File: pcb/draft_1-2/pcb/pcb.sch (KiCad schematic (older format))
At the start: 26 parts, among them J1 USB4110-GF-A, U1 H3LIS200DLTR, U2 ATSAML21J16B-AUT, U3 BQ25155

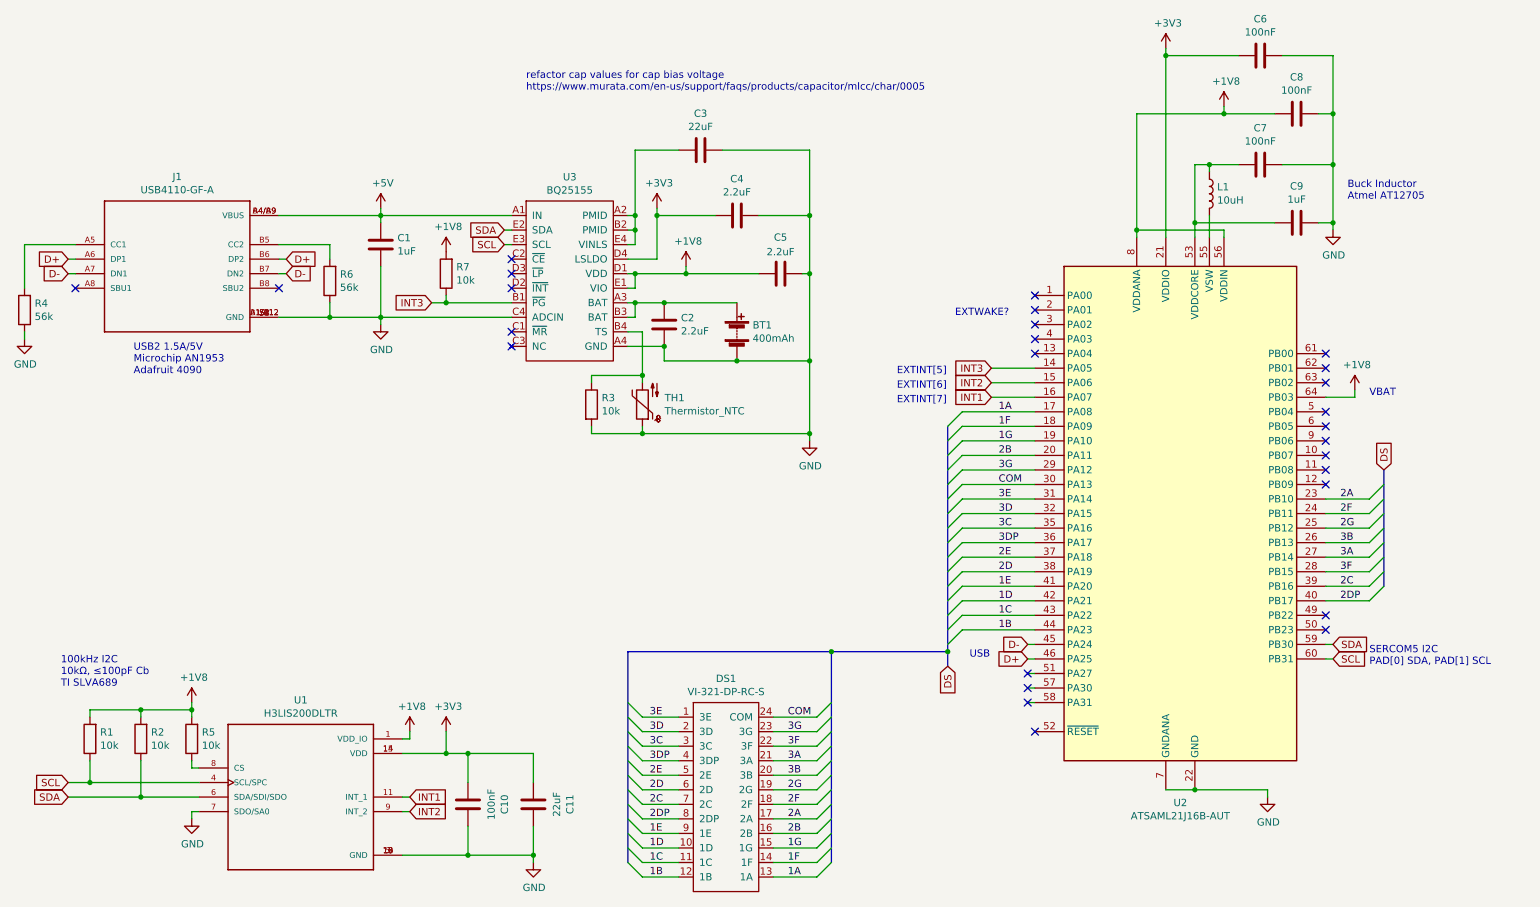
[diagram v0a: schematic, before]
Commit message: organized silk screen and swd tp
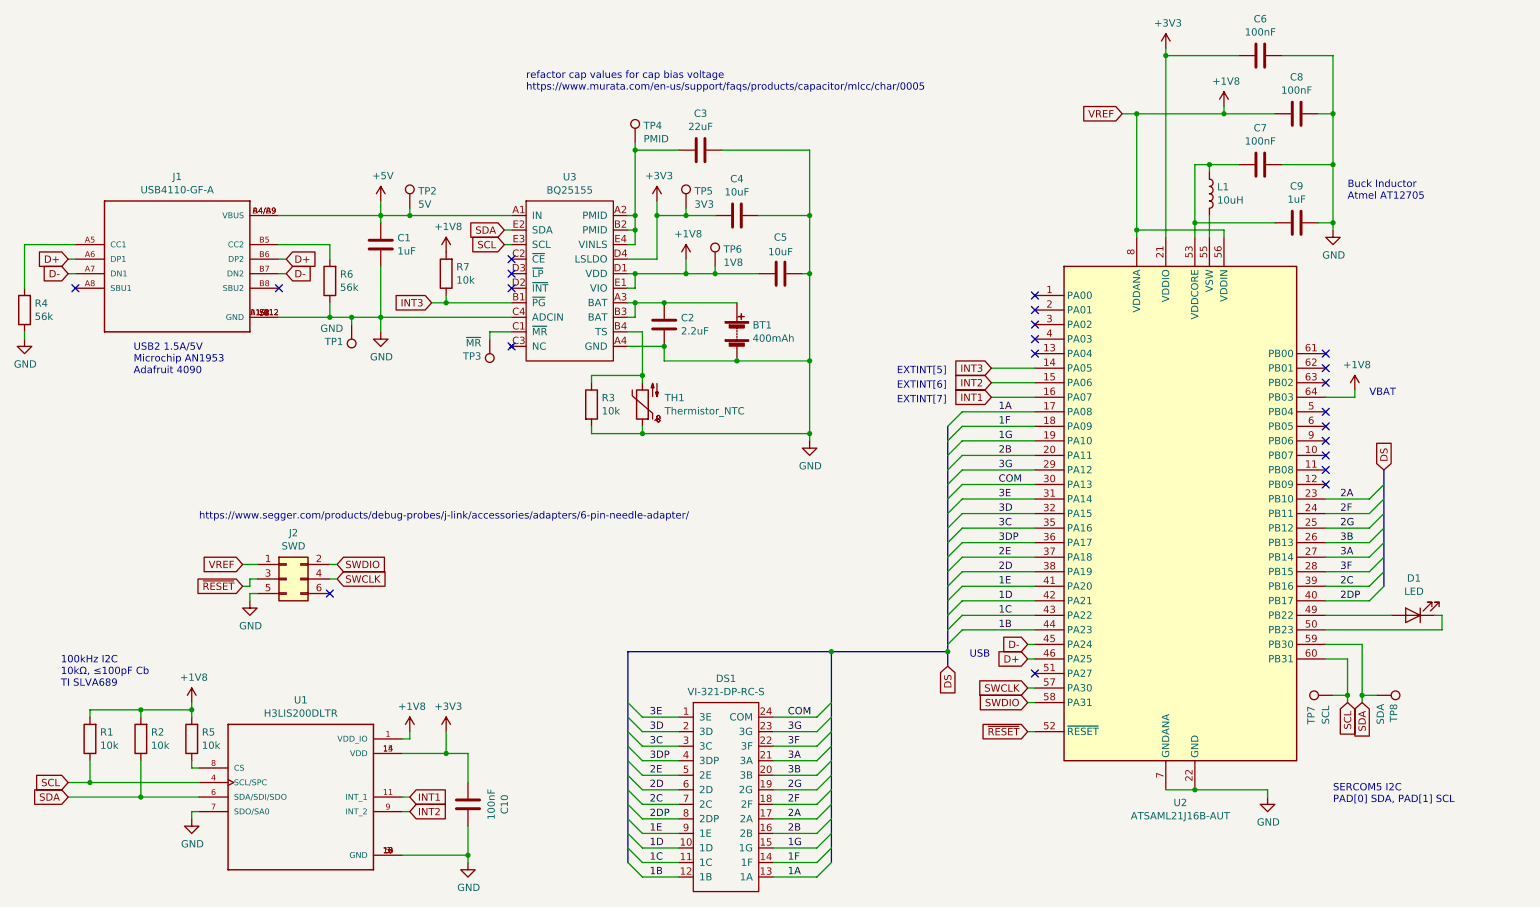
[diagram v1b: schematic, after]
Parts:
- removed C11: 22uF, Capacitor_SMD:C_0805_2012Metric, symbol Device:C
- added D1: LED, LED_SMD:LED_0603_1608Metric_Castellated, symbol Device:LED
- added J2: SWD, Connector_PinHeader_2.54mm:PinHeader_2x03_P2.54mm_Vertical, symbol Connector_Generic:Conn_02x03_Odd_Even
- added TP1: GND, symbol Connector:TestPoint
- added TP2: 5V, symbol Connector:TestPoint
- added TP3: ~MR, symbol Connector:TestPoint
- added TP4: PMID, symbol Connector:TestPoint
- added TP5: 3V3, symbol Connector:TestPoint
- added TP6: 1V8, symbol Connector:TestPoint
- added TP7: SCL, symbol Connector:TestPoint
- added TP8: SDA, symbol Connector:TestPoint
- C4, C5: value 2.2uF -> 10uF
- TH1: footprint Resistor_SMD:R_0402_1005Metric -> Connector_PinHeader_2.54mm:PinHeader_1x02_P2.54mm_Vertical
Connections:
- net +1V8: now also J2.1 (Pin_1), TP6.1
- net +3V3: now also TP5.1
- net +5V: now also TP2.1
- net GND: now also J2.5 (Pin_5), TP1.1
- net SCL: now also TP7.1
- net SDA: now also TP8.1
- net at C3.2, U3.A2 (PMID), U3.B2 (PMID)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: now also TP4.1
- net at U3.C1 (~MR): now also TP3.1
- net at U2.49 (PB22): now also D1.2 (A)
- net at U2.50 (PB23): now also D1.1 (K)
- net ~RESET: now reaches U2.52 (~RESET)
- net ~RESET: now also J2.3 (Pin_3)
- net SWCLK: now reaches U2.57 (PA30)
- net SWCLK: now also J2.4 (Pin_4)
- net SWDIO: now reaches U2.58 (PA31)
- net SWDIO: now also J2.2 (Pin_2)
- no-connect marks 27 -> 22
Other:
- note added: "https://www.segger.com/products/debug-probes/j-link/accessories/adapters/6-pin-needle-adapter/"
- note removed: "EXTWAKE?"

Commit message: add example image to readme
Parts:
- C1, C10, C2, C4, C5, C6, C7, C8, C9: footprint Capacitor_SMD:C_0402_1005Metric -> Capacitor_SMD:C_0805_2012Metric
- R1, R2, R3, R4, R5, R6, R7: footprint Resistor_SMD:R_0402_1005Metric -> Resistor_SMD:R_0805_2012Metric
- TP1, TP2, TP3, TP4, TP5, TP6, TP7, TP8: footprint (none) -> TestPoint:TestPoint_Pad_2.0x2.0mm
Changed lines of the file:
@@
 F 0 "R5" H 1930 5504 50  0000 R CNN
 F 1 "10k" H 1930 5595 50  0000 R CNN
-F 2 "Resistor_SMD:R_0402_1005Metric" V 1930 5550 50  0001 C CNN
+F 2 "Resistor_SMD:R_0805_2012Metric" V 1930 5550 50  0001 C CNN
 F 3 "~" H 2000 5550 50  0001 C CNN
 	1    2000 5550
@@
 F 0 "C1" H 3415 2196 50  0000 L CNN
 F 1 "1uF" H 3415 2105 50  0000 L CNN
-F 2 "Capacitor_SMD:C_0402_1005Metric" H 3338 2000 50  0001 C CNN
+F 2 "Capacitor_SMD:C_0805_2012Metric" H 3338 2000 50  0001 C CNN
 F 3 "~" H 3300 2150 50  0001 C CNN
 	1    3300 2150
@@
 F 0 "C5" V 6300 2350 50  0000 C CNN
 F 1 "10uF" V 6200 2350 50  0000 C CNN
-F 2 "Capacitor_SMD:C_0402_1005Metric" H 6088 2200 50  0001 C CNN
+F 2 "Capacitor_SMD:C_0805_2012Metric" H 6088 2200 50  0001 C CNN
 F 3 "~" H 6050 2350 50  0001 C CNN
 	1    6050 2350
@@
 F 0 "C2" H 5365 2746 50  0000 L CNN
 F 1 "2.2uF" H 5365 2655 50  0000 L CNN
-F 2 "Capacitor_SMD:C_0402_1005Metric" H 5288 2550 50  0001 C CNN
+F 2 "Capacitor_SMD:C_0805_2012Metric" H 5288 2550 50  0001 C CNN
 F 3 "~" H 5250 2700 50  0001 C CNN
 	1    5250 2700
@@
 F 0 "R3" H 4820 3296 50  0000 L CNN
 F 1 "10k" H 4820 3205 50  0000 L CNN
-F 2 "Resistor_SMD:R_0402_1005Metric" V 4680 3250 50  0001 C CNN
+F 2 "Resistor_SMD:R_0805_2012Metric" V 4680 3250 50  0001 C CNN
 F 3 "~" H 4750 3250 50  0001 C CNN
 	1    4750 3250
@@
 F 0 "R6" H 2880 2354 50  0000 R CNN
 F 1 "56k" H 2880 2445 50  0000 R CNN
-F 2 "Resistor_SMD:R_0402_1005Metric" V 2880 2400 50  0001 C CNN
+F 2 "Resistor_SMD:R_0805_2012Metric" V 2880 2400 50  0001 C CNN
 F 3 "~" H 2950 2400 50  0001 C CNN
 	1    2950 2400
@@
 F 0 "R7" H 3680 2304 50  0000 R CNN
 F 1 "10k" H 3680 2395 50  0000 R CNN
-F 2 "Resistor_SMD:R_0402_1005Metric" V 3680 2350 50  0001 C CNN
+F 2 "Resistor_SMD:R_0805_2012Metric" V 3680 2350 50  0001 C CNN
 F 3 "~" H 3750 2350 50  0001 C CNN
 	1    3750 2350
@@
 F 0 "R4" H 780 2554 50  0000 R CNN
 F 1 "56k" H 780 2645 50  0000 R CNN
-F 2 "Resistor_SMD:R_0402_1005Metric" V 780 2600 50  0001 C CNN
+F 2 "Resistor_SMD:R_0805_2012Metric" V 780 2600 50  0001 C CNN
 F 3 "~" H 850 2600 50  0001 C CNN
 	1    850  2600
@@
 F 0 "C8" V 9852 1250 50  0000 C CNN
 F 1 "100nF" V 9761 1250 50  0000 C CNN
-F 2 "Capacitor_SMD:C_0402_1005Metric" H 9638 1100 50  0001 C CNN
+F 2 "Capacitor_SMD:C_0805_2012Metric" H 9638 1100 50  0001 C CNN
 F 3 "~" H 9600 1250 50  0001 C CNN
 	1    9600 1250
@@
 F 0 "C6" V 9602 850 50  0000 C CNN
 F 1 "100nF" V 9511 850 50  0000 C CNN
-F 2 "Capacitor_SMD:C_0402_1005Metric" H 9388 700 50  0001 C CNN
+F 2 "Capacitor_SMD:C_0805_2012Metric" H 9388 700 50  0001 C CNN
 F 3 "~" H 9350 850 50  0001 C CNN
 	1    9350 850
@@
 F 0 "C9" V 9852 2000 50  0000 C CNN
 F 1 "1uF" V 9761 2000 50  0000 C CNN
-F 2 "Capacitor_SMD:C_0402_1005Metric" H 9638 1850 50  0001 C CNN
+F 2 "Capacitor_SMD:C_0805_2012Metric" H 9638 1850 50  0001 C CNN
 F 3 "~" H 9600 2000 50  0001 C CNN
 	1    9600 2000
@@
 F 0 "C7" V 9602 1600 50  0000 C CNN
 F 1 "100nF" V 9511 1600 50  0000 C CNN
-F 2 "Capacitor_SMD:C_0402_1005Metric" H 9388 1450 50  0001 C CNN
+F 2 "Capacitor_SMD:C_0805_2012Metric" H 9388 1450 50  0001 C CNN
 F 3 "~" H 9350 1600 50  0001 C CNN
 	1    9350 1600
@@
 F 0 "R2" H 1580 5504 50  0000 R CNN
 F 1 "10k" H 1580 5595 50  0000 R CNN
-F 2 "Resistor_SMD:R_0402_1005Metric" V 1580 5550 50  0001 C CNN
+F 2 "Resistor_SMD:R_0805_2012Metric" V 1580 5550 50  0001 C CNN
 F 3 "~" H 1650 5550 50  0001 C CNN
 	1    1650 5550
@@
 F 0 "R1" H 1230 5504 50  0000 R CNN
 F 1 "10k" H 1230 5595 50  0000 R CNN
-F 2 "Resistor_SMD:R_0402_1005Metric" V 1230 5550 50  0001 C CNN
+F 2 "Resistor_SMD:R_0805_2012Metric" V 1230 5550 50  0001 C CNN
 F 3 "~" H 1300 5550 50  0001 C CNN
 	1    1300 5550
@@
 F 0 "C4" V 6002 1950 50  0000 C CNN
 F 1 "10uF" V 5911 1950 50  0000 C CNN
-F 2 "Capacitor_SMD:C_0402_1005Metric" H 5788 1800 50  0001 C CNN
+F 2 "Capacitor_SMD:C_0805_2012Metric" H 5788 1800 50  0001 C CNN
 F 3 "~" H 5750 1950 50  0001 C CNN
 	1    5750 1950
@@
 F 0 "C10" V 3648 6000 50  0000 C CNN
 F 1 "100nF" V 3739 6000 50  0000 C CNN
-F 2 "Capacitor_SMD:C_0402_1005Metric" H 3938 5850 50  0001 C CNN
+F 2 "Capacitor_SMD:C_0805_2012Metric" H 3938 5850 50  0001 C CNN
 F 3 "~" H 3900 6000 50  0001 C CNN
 	1    3900 6000
@@
 F 0 "TP2" H 3558 2018 50  0000 L CNN
 F 1 "5V" H 3558 1927 50  0000 L CNN
-F 2 "" H 3700 1900 50  0001 C CNN
+F 2 "TestPoint:TestPoint_Pad_2.0x2.0mm" H 3700 1900 50  0001 C CNN
 F 3 "~" H 3700 1900 50  0001 C CNN
 	1    3500 1900
@@
 F 0 "TP6" H 5658 2418 50  0000 L CNN
 F 1 "1V8" H 5658 2327 50  0000 L CNN
-F 2 "" H 5800 2300 50  0001 C CNN
+F 2 "TestPoint:TestPoint_Pad_2.0x2.0mm" H 5800 2300 50  0001 C CNN
 F 3 "~" H 5800 2300 50  0001 C CNN
 	1    5600 2300
@@
 F 0 "TP1" H 3158 2818 50  0000 L CNN
 F 1 "GND" H 3158 2727 50  0000 L CNN
-F 2 "" H 3300 2700 50  0001 C CNN
+F 2 "TestPoint:TestPoint_Pad_2.0x2.0mm" H 3300 2700 50  0001 C CNN
 F 3 "~" H 3300 2700 50  0001 C CNN
 	1    3100 2700
@@
 F 0 "TP8" H 10208 5368 50  0000 L CNN
 F 1 "SDA" H 10208 5277 50  0000 L CNN
-F 2 "" H 10350 5250 50  0001 C CNN
+F 2 "TestPoint:TestPoint_Pad_2.0x2.0mm" H 10350 5250 50  0001 C CNN
 F 3 "~" H 10350 5250 50  0001 C CNN
 	1    10150 5250
@@
 F 0 "TP7" H 9650 5400 50  0000 L CNN
 F 1 "SCL" H 9650 5300 50  0000 L CNN
-F 2 "" H 10050 5250 50  0001 C CNN
+F 2 "TestPoint:TestPoint_Pad_2.0x2.0mm" H 10050 5250 50  0001 C CNN
 F 3 "~" H 10050 5250 50  0001 C CNN
 	1    9850 5250
@@
 F 0 "TP4" H 5108 1568 50  0000 L CNN
 F 1 "PMID" H 5108 1477 50  0000 L CNN
-F 2 "" H 5250 1450 50  0001 C CNN
+F 2 "TestPoint:TestPoint_Pad_2.0x2.0mm" H 5250 1450 50  0001 C CNN
 F 3 "~" H 5250 1450 50  0001 C CNN
 	1    5050 1450
@@
 F 0 "TP5" H 5458 2018 50  0000 L CNN
 F 1 "3V3" H 5458 1927 50  0000 L CNN
-F 2 "" H 5600 1900 50  0001 C CNN
+F 2 "TestPoint:TestPoint_Pad_2.0x2.0mm" H 5600 1900 50  0001 C CNN
 F 3 "~" H 5600 1900 50  0001 C CNN
 	1    5400 1900
@@
 F 0 "TP3" H 4108 2918 50  0000 L CNN
 F 1 "~MR" H 4108 2827 50  0000 L CNN
-F 2 "" H 4250 2800 50  0001 C CNN
+F 2 "TestPoint:TestPoint_Pad_2.0x2.0mm" H 4250 2800 50  0001 C CNN
 F 3 "~" H 4250 2800 50  0001 C CNN
 	1    4050 2800

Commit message: v1.2 draft
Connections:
- net INT1: now also U2.14 (PA05); no longer U2.16 (PA07)
- net INT3: now also U2.16 (PA07); no longer U2.14 (PA05)
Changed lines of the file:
@@
 Wire Wire Line
 	8900 2000 9450 2000
-Text GLabel 7500 3200 0    50   Input ~ 0
+Text GLabel 7500 3000 0    50   Input ~ 0
 INT1
 Text GLabel 7500 3100 0    50   Input ~ 0
 INT2
-Text GLabel 7500 3000 0    50   Input ~ 0
+Text GLabel 7500 3200 0    50   Input ~ 0
 INT3
 Text GLabel 10050 5300 3    50   Input ~ 0
